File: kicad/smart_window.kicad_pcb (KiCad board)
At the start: 2 copper layers, 73.5 x 56 mm, 27 parts, among them J1 PROG, J10 LS2, J12 LS3, J13 Vmot1, J3 DOOR1, J4 MOT2, J5 MOT1, J6 MOT3, J7 I2C, J8 DOOR2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

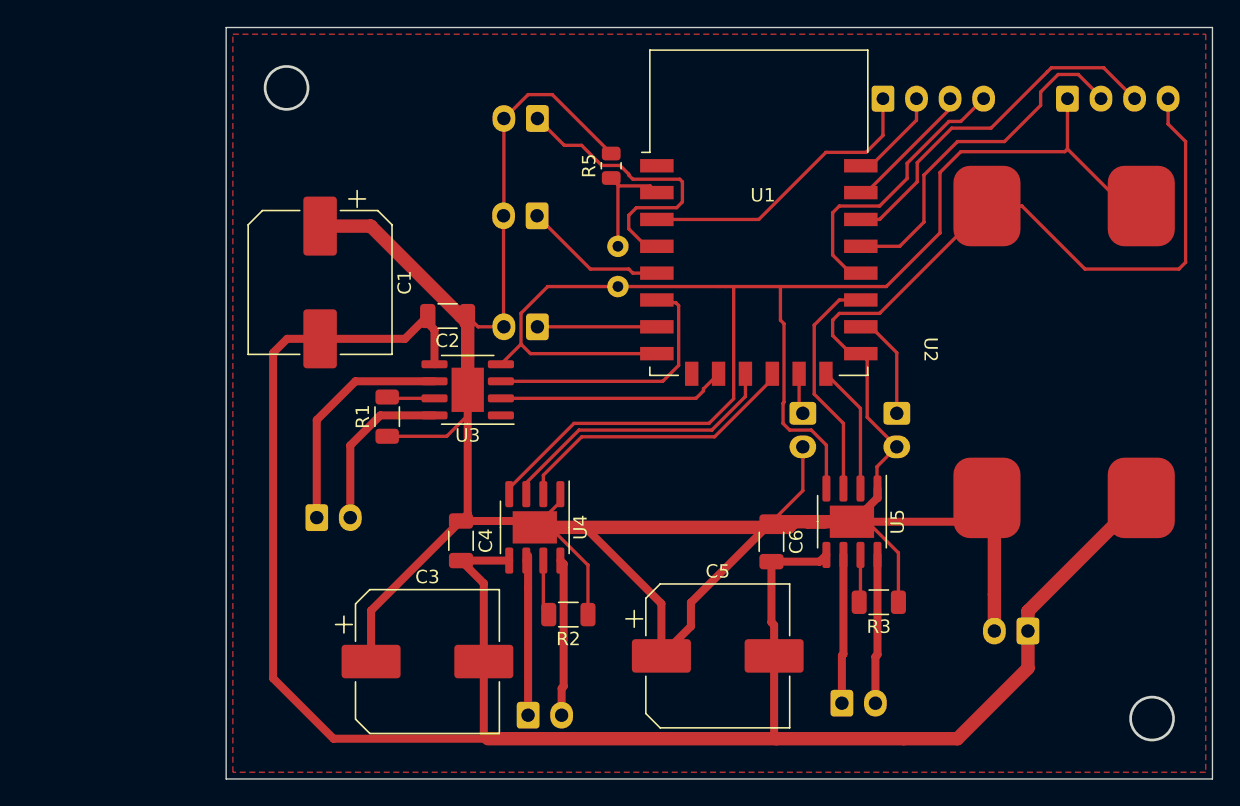
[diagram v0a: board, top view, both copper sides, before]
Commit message: 2-сторонняя версия
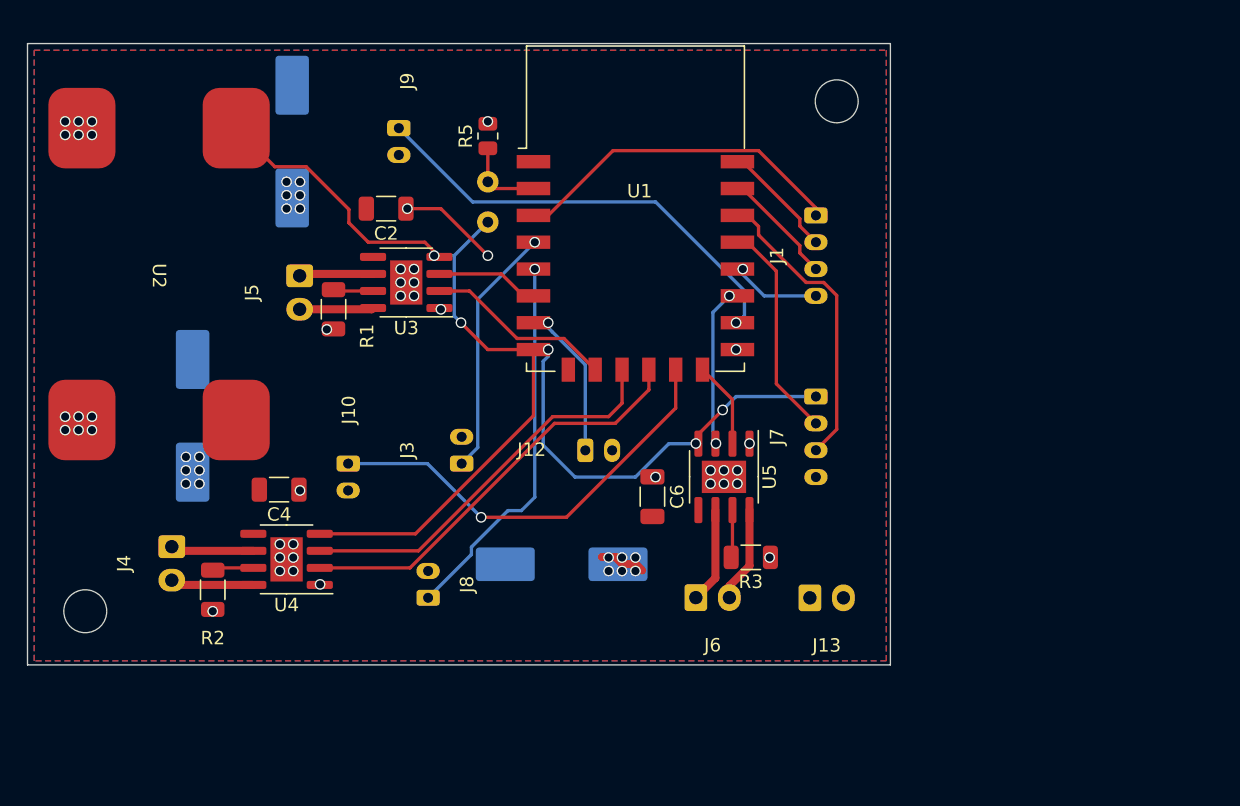
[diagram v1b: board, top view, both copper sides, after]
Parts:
- added H1: MountingHole, MountingHole:MountingHole_3.2mm_M3, F.Cu at (18.5, 56.0)
- added H2: MountingHole, MountingHole:MountingHole_3.2mm_M3, F.Cu at (74.5, 18.0)
- C1, C3, C5: moved to B.Cu
- J1, J7: footprint Connector_JST:JST_XH_B4B-XH-A_1x04_P2.50mm_Vertical -> Connector_JST:JST_PH_B4B-PH-K_1x04_P2.00mm_Vertical
- J10, J12, J3, J8, J9: footprint Connector_JST:JST_XH_B2B-XH-A_1x02_P2.50mm_Vertical -> Connector_JST:JST_PH_B2B-PH-K_1x02_P2.00mm_Vertical
- moved U2 67.7 mm to (24.0, 31.0)
- moved J9 42.8 mm to (41.9, 20.0)
- moved J10 34.1 mm to (38.1, 45.0)
- moved J8 29.6 mm to (44.0, 55.0), turned to 90 degrees
- moved J4 29.4 mm to (24.9, 51.2), turned to -90 degrees
- moved J7 29.1 mm to (73.0, 40.0), turned to -90 degrees
- moved R2 26.6 mm to (28.0, 54.4), turned to 90 degrees
- moved J3 26.3 mm to (46.5, 45.0), turned to 90 degrees
- moved C3 25.3 mm to (26.5, 41.4), turned to -90 degrees
- moved U4 18.7 mm to (33.5, 52.1), turned to 180 degrees
- moved J5 18.1 mm to (34.5, 31.0), turned to -90 degrees
- moved J13 16.4 mm to (72.5, 55.0), turned to 0 degrees
- moved C4 14.1 mm to (32.9, 46.9), turned to 180 degrees
- moved C5 13.5 mm to (54.0, 52.5)
- moved J6 13.4 mm to (64.0, 55.0)
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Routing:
- net GND: track 260.8 -> 10.0 mm, vias 0 -> 42
- net /24V+: track 152.9 -> 3.94 mm, vias 0 -> 18
- net /M2_LS: track 3.06 -> 32.3 mm, vias 0 -> 1
- net +3V3: track 118.8 -> 92.4 mm, vias 0 -> 5
- net /M1_LS: track 7.99 -> 33.4 mm, vias 0 -> 1
- net /DOOR2: track 10.7 -> 28.4 mm, vias 0 -> 1
- net /ESP_GPIO0: track 21.2 -> 6.68 mm, vias 0 -> 1
- net /M1_EN: track 21.6 -> 7.68 mm
- net Net-(J5-Pad1): track 17.2 -> 5.89 mm
- net /SDA: track 26.7 -> 16.4 mm
- net /M2_DIR: track 21.8 -> 31.5 mm
- net /M2_EN: track 21.5 -> 29.6 mm
- net Net-(J5-Pad2): track 12.6 -> 6.01 mm
- net Net-(J4-Pad1): track 12.3 -> 6.21 mm
- net Net-(J4-Pad2): track 11.7 -> 5.73 mm
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- added copper zone on F.Cu, net /24V+
- added copper zone on B.Cu, net GND
- removed copper zone on F.Cu, net GND
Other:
- board size 73.5 x 56 mm -> 64.3 x 46.3 mm
- board text added: "@klaus_schwartz, Чебоксары, Январь 2023"
- board text added: "Контроллер умного окна"
